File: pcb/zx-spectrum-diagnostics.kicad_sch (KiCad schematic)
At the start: 18 parts, among them U101 Pico, U102 ICL7660, U103 LM321

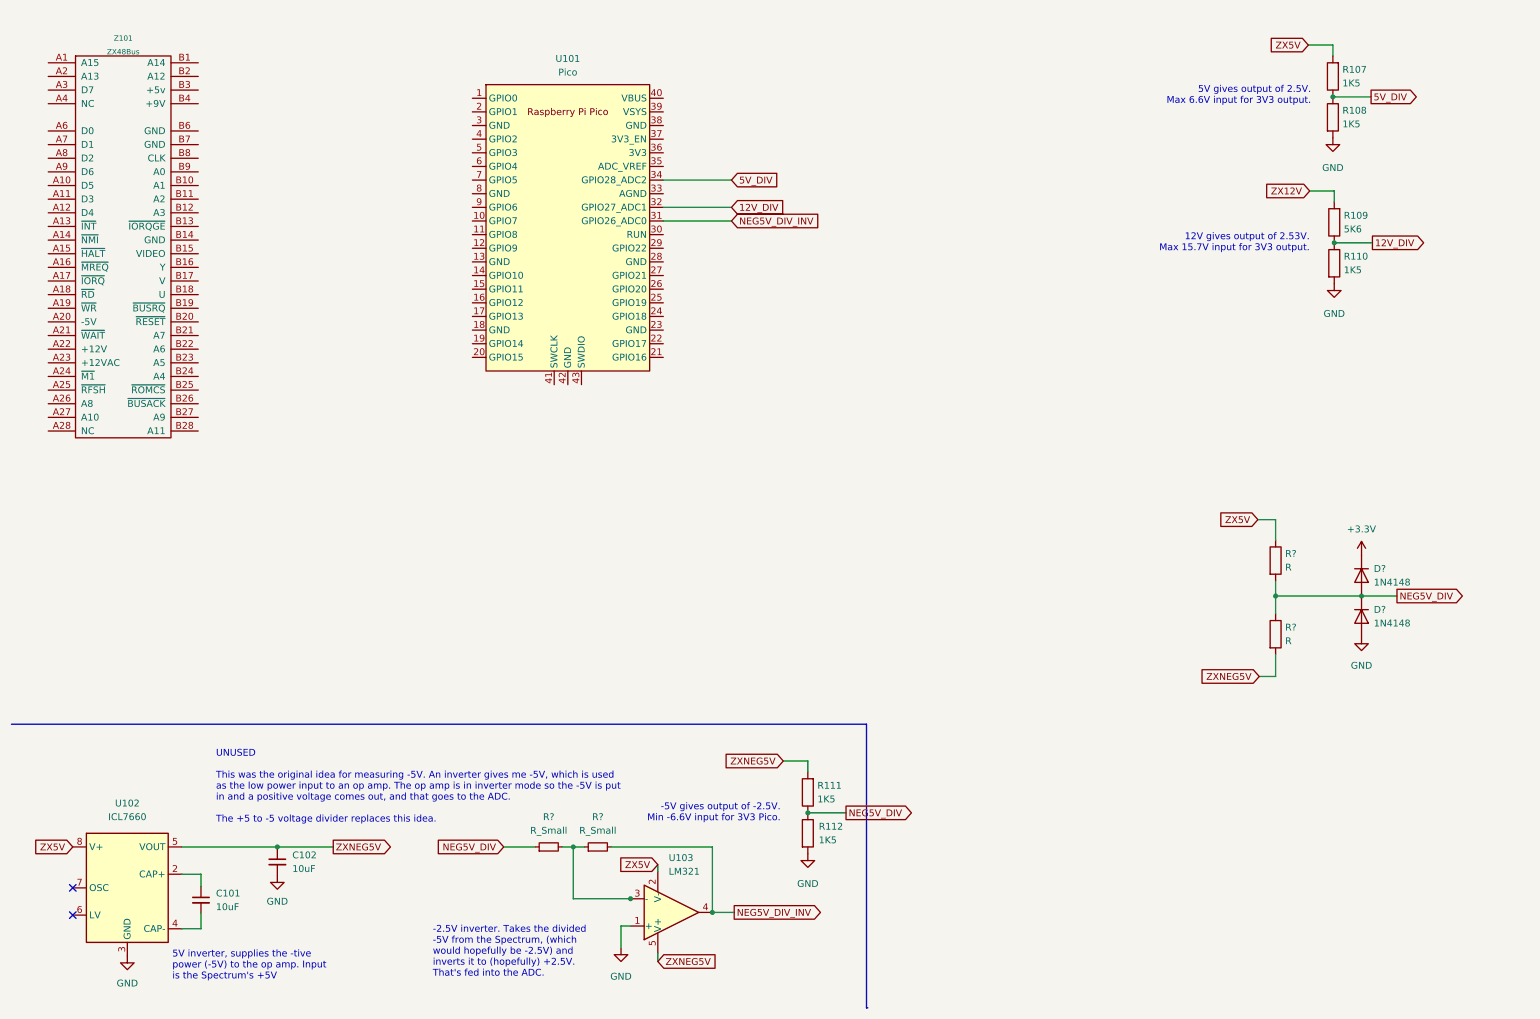
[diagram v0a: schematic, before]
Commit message: update schematic, add a second pico, tidy -5V sampler
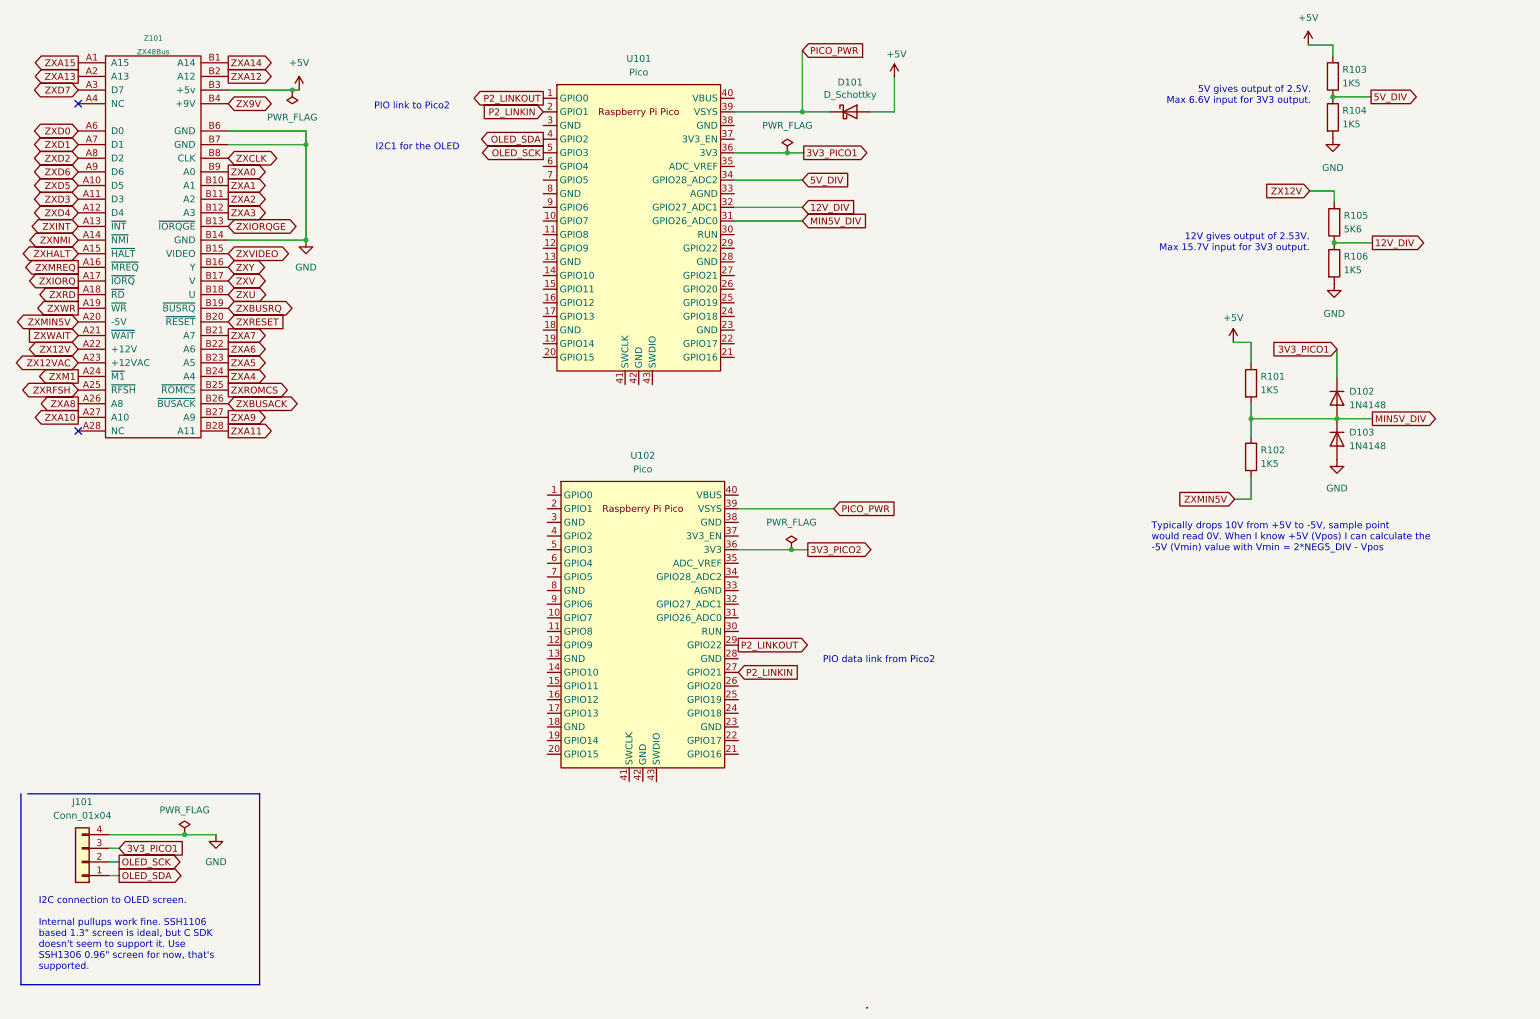
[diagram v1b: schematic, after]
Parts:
- removed C101, C102: 10uF, symbol Device:C_Small
- removed R111, R112: 1K5, symbol Device:R
- removed R? (x2): R_Small, symbol Device:R_Small
- removed U102: ICL7660, Package_SO:SOIC-8-N7_3.9x4.9mm_P1.27mm, symbol Regulator_SwitchedCapacitor:ICL7660
- removed U103: LM321, Package_TO_SOT_SMD:SOT-23-5, symbol Amplifier_Operational:LM321
- added D101: D_Schottky, Diode_SMD:D_1206_3216Metric_Pad1.42x1.75mm_HandSolder, symbol Device:D_Schottky
- added J101: Conn_01x04, symbol Connector_Generic:Conn_01x04
- added U102: Pico, RPi_Pico:RPi_Pico_SMD_TH, symbol Pico:Pico
- R101, R102: renamed from R?; value R -> 1K5
- gave numbers to parts that had none: 2
- renumbered R107 to R103, R108 to R104, R109 to R105, R110 to R106
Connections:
- net +3.3V is gone; now on net 3V3_PICO1: D102.1 (K)
- net NEG5V_DIV_INV is gone; now on net MIN5V_DIV: U101.31 (GPIO26_ADC0)
- net ZX5V is gone; now on net +5V: R101.1, R103.2
- net ZXNEG5V is gone; now on net ZXMIN5V: R102.2
- net GND: now also Z101.B14 (GND), Z101.B6 (GND), Z101.B7 (GND), J101.4 (Pin_4)
- net ZX12V: now also Z101.A22 (+12V)
- net ZXA15: now reaches Z101.A1 (A15)
- net ZXD5: now reaches Z101.A10 (D5)
- net ZXD3: now reaches Z101.A11 (D3)
- net ZXD4: now reaches Z101.A12 (D4)
- net ZXINT: now reaches Z101.A13 (~{INT})
- net ZXNMI: now reaches Z101.A14 (~{NMI})
- net ZXHALT: now reaches Z101.A15 (~{HALT})
- net ZXMREQ: now reaches Z101.A16 (~{MREQ})
- net ZXIORQ: now reaches Z101.A17 (~{IORQ})
- net ZXRD: now reaches Z101.A18 (~{RD})
- net ZXWR: now reaches Z101.A19 (~{WR})
- net ZXA13: now reaches Z101.A2 (A13)
- net ZXMIN5V: now reaches Z101.A20 (-5V)
- net ZXWAIT: now reaches Z101.A21 (~{WAIT})
- net ZX12VAC: now reaches Z101.A23 (+12VAC)
- net ZXM1: now reaches Z101.A24 (~{M1})
- net ZXRFSH: now reaches Z101.A25 (~{RFSH})
- net ZXA8: now reaches Z101.A26 (A8)
- net ZXA10: now reaches Z101.A27 (A10)
- net ZXD7: now reaches Z101.A3 (D7)
- net ZXD0: now reaches Z101.A6 (D0)
- net ZXD1: now reaches Z101.A7 (D1)
- net ZXD2: now reaches Z101.A8 (D2)
- net ZXD6: now reaches Z101.A9 (D6)
- net ZXA14: now reaches Z101.B1 (A14)
- net ZXA1: now reaches Z101.B10 (A1)
- net ZXA2: now reaches Z101.B11 (A2)
- net ZXA3: now reaches Z101.B12 (A3)
- net ZXIORQGE: now reaches Z101.B13 (~{IORQGE})
- net ZXVIDEO: now reaches Z101.B15 (VIDEO)
- net ZXY: now reaches Z101.B16 (Y)
- net ZXV: now reaches Z101.B17 (V)
- net ZXU: now reaches Z101.B18 (U)
- net ZXBUSRQ: now reaches Z101.B19 (~{BUSRQ})
- net ZXA12: now reaches Z101.B2 (A12)
- net ZXRESET: now reaches Z101.B20 (~{RESET})
- net ZXA7: now reaches Z101.B21 (A7)
- net ZXA6: now reaches Z101.B22 (A6)
- net ZXA5: now reaches Z101.B23 (A5)
- net ZXA4: now reaches Z101.B24 (A4)
- net ZXROMCS: now reaches Z101.B25 (~{ROMCS})
- net ZXBUSACK: now reaches Z101.B26 (~{BUSACK})
- net ZXA9: now reaches Z101.B27 (A9)
- net ZXA11: now reaches Z101.B28 (A11)
- net +5V: now reaches Z101.B3 (+5v)
- net +5V: now also D101.2 (A)
- net ZX9V: now reaches Z101.B4 (+9V)
- net ZXCLK: now reaches Z101.B8 (CLK)
- net ZXA0: now reaches Z101.B9 (A0)
- net P2_LINKOUT: now reaches U101.1 (GPIO0)
- net P2_LINKOUT: now also U102.29 (GPIO22)
- net P2_LINKIN: now reaches U101.2 (GPIO1)
- net P2_LINKIN: now also U102.27 (GPIO21)
- net 3V3_PICO1: now reaches U101.36 (3V3)
- net 3V3_PICO1: now also J101.3 (Pin_3)
- net PICO_PWR: now reaches U101.39 (VSYS)
- net PICO_PWR: now also D101.1 (K), U102.39 (VSYS)
- net OLED_SDA: now reaches U101.4 (GPIO2)
- net OLED_SDA: now also J101.1 (Pin_1)
- net OLED_SCK: now reaches U101.5 (GPIO3)
- net OLED_SCK: now also J101.2 (Pin_2)
- net NEG5V_DIV renamed MIN5V_DIV
- new net 3V3_PICO2: U102.36 (3V3)
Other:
- note added: "I2C connection to OLED screen. Internal pullups work fine. SSH1106 based 1.3" screen is ideal, but C SDK doesn't seem to support it. Use SSH1306 0.96" screen for now, that's supported."
- note added: "I2C1 for the OLED"
- note added: "PIO data link from Pico2"
- note added: "PIO link to Pico2"
- note added: "Typically drops 10V from +5V to -5V, sample point would read 0V. When I know +5V (Vpos) I can calculate the -5V (Vmin) value with Vmin = 2*NEG5_DIV - Vpos"
- note removed: "-2.5V inverter. Takes the divided -5V from the Spectrum, (which would hopefully be -2.5V) and inverts it to (hopefully) +2.5V. That's fed into the ADC."
- note removed: "-5V gives output of -2.5V. Min -6.6V input for 3V3 Pico."
- note removed: "5V inverter, supplies the -tive power (-5V) to the op amp. Input is the Spectrum's +5V"
- note removed: "UNUSED This was the original idea for measuring -5V. An inverter gives me -5V, which is used as the low power input to an op amp. The op amp is in inverter mode so the -5V is put in and a positive voltage comes out, and that goes to the ADC. The +5 to -5 voltage divider replaces this idea."
- moved on the sheet: D102, D103, R101, R102, U101, Z101

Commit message: first layout
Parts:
- D102, D103: footprint Diode_THT:D_DO-35_SOD27_P7.62mm_Horizontal -> Diode_SMD:D_1206_3216Metric_Pad1.42x1.75mm_HandSolder
- J101: footprint (none) -> Connector_PinHeader_2.54mm:PinHeader_1x04_P2.54mm_Vertical
- R101, R102, R103, R104, R105, R106: footprint (none) -> Resistor_SMD:R_1206_3216Metric_Pad1.30x1.75mm_HandSolder
- U101, U102: footprint RPi_Pico:RPi_Pico_SMD_TH -> Pico:RPi_Pico_SMD_TH
- Z101: footprint (none) -> zxbus:ZX_Bus_Pin_Header
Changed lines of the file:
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@@
   (title_block
     (title "ZX Spectrum Diagnostics Board")
-    (date "2023-08-27")
+    (date "2023-10-29")
   )
   (junction (at 67.818 37.592) (diameter 0) (color 0 0 0 0)
@@
       (effects (font (size 0.9906 0.9906)))
     )
-    (property "Footprint" "" (id 2) (at 30.48 103.632 0)
+    (property "Footprint" "zxbus:ZX_Bus_Pin_Header" (id 2) (at 30.48 103.632 0)
       (effects (font (size 0.9906 0.9906)) hide)
     )
@@
     (property "Reference" "J101" (id 0) (at 26.162 160.02 0))
     (property "Value" "Conn_01x04" (id 1) (at 26.162 162.56 0))
-    (property "Footprint" "" (id 2) (at 26.162 171.196 0)
+    (property "Footprint" "Connector_PinHeader_2.54mm:PinHeader_1x04_P2.54mm_Vertical" (id 2) (at 26.162 171.196 0)
       (effects (font (size 1.27 1.27)) hide)
     )
@@
     (property "Reference" "U101" (id 0) (at 129.794 21.59 0))
     (property "Value" "Pico" (id 1) (at 129.794 24.13 0))
-    (property "Footprint" "RPi_Pico:RPi_Pico_SMD_TH" (id 2) (at 129.794 53.086 90)
+    (property "Footprint" "Pico:RPi_Pico_SMD_TH" (id 2) (at 129.794 53.086 90)
       (effects (font (size 1.27 1.27)) hide)
     )
@@
       (effects (font (size 1.27 1.27)) (justify right))
     )
-    (property "Footprint" "" (id 2) (at 261.112 52.07 90)
+    (property "Footprint" "Resistor_SMD:R_1206_3216Metric_Pad1.30x1.75mm_HandSolder" (id 2) (at 261.112 52.07 90)
       (effects (font (size 1.27 1.27)) hide)
     )
@@
     (property "Reference" "U102" (id 0) (at 130.556 95.504 0))
     (property "Value" "Pico" (id 1) (at 130.556 98.044 0))
-    (property "Footprint" "RPi_Pico:RPi_Pico_SMD_TH" (id 2) (at 130.556 127 90)
+    (property "Footprint" "Pico:RPi_Pico_SMD_TH" (id 2) (at 130.556 127 90)
       (effects (font (size 1.27 1.27)) hide)
     )
@@
       (effects (font (size 1.27 1.27)) (justify right))
     )
-    (property "Footprint" "" (id 2) (at 260.858 24.892 90)
+    (property "Footprint" "Resistor_SMD:R_1206_3216Metric_Pad1.30x1.75mm_HandSolder" (id 2) (at 260.858 24.892 90)
       (effects (font (size 1.27 1.27)) hide)
     )
@@
       (effects (font (size 1.27 1.27)) (justify left))
     )
-    (property "Footprint" "Diode_THT:D_DO-35_SOD27_P7.62mm_Horizontal" (id 2) (at 259.842 92.456 0)
+    (property "Footprint" "Diode_SMD:D_1206_3216Metric_Pad1.42x1.75mm_HandSolder" (id 2) (at 259.842 92.456 0)
       (effects (font (size 1.27 1.27)) hide)
     )
@@
       (effects (font (size 1.27 1.27)) (justify left))
     )
-    (property "Footprint" "Diode_THT:D_DO-35_SOD27_P7.62mm_Horizontal" (id 2) (at 259.842 84.836 0)
+    (property "Footprint" "Diode_SMD:D_1206_3216Metric_Pad1.42x1.75mm_HandSolder" (id 2) (at 259.842 84.836 0)
       (effects (font (size 1.27 1.27)) hide)
     )
@@
       (effects (font (size 1.27 1.27)) (justify left))
     )
-    (property "Footprint" "" (id 2) (at 242.062 95.758 90)
+    (property "Footprint" "Resistor_SMD:R_1206_3216Metric_Pad1.30x1.75mm_HandSolder" (id 2) (at 242.062 95.758 90)
       (effects (font (size 1.27 1.27)) hide)
     )
@@
       (effects (font (size 1.27 1.27)) (justify left))
     )
-    (property "Footprint" "" (id 2) (at 257.302 32.512 90)
+    (property "Footprint" "Resistor_SMD:R_1206_3216Metric_Pad1.30x1.75mm_HandSolder" (id 2) (at 257.302 32.512 90)
       (effects (font (size 1.27 1.27)) hide)
     )
@@
       (effects (font (size 1.27 1.27)) (justify left))
     )
-    (property "Footprint" "" (id 2) (at 242.062 82.042 90)
+    (property "Footprint" "Resistor_SMD:R_1206_3216Metric_Pad1.30x1.75mm_HandSolder" (id 2) (at 242.062 82.042 90)
       (effects (font (size 1.27 1.27)) hide)
     )
@@
       (effects (font (size 1.27 1.27)) (justify left))
     )
-    (property "Footprint" "" (id 2) (at 257.556 59.69 90)
+    (property "Footprint" "Resistor_SMD:R_1206_3216Metric_Pad1.30x1.75mm_HandSolder" (id 2) (at 257.556 59.69 90)
       (effects (font (size 1.27 1.27)) hide)
     )
@@
     )
     (path "/d9d4c412-10f6-47b7-9c11-43e0dd422b75"
-      (reference "D102") (unit 1) (value "1N4148") (footprint "Diode_THT:D_DO-35_SOD27_P7.62mm_Horizontal")
+      (reference "D102") (unit 1) (value "1N4148") (footprint "Diode_SMD:D_1206_3216Metric_Pad1.42x1.75mm_HandSolder")
     )
     (path "/d3364c3f-7456-4539-86a5-d88591e950f5"
-      (reference "D103") (unit 1) (value "1N4148") (footprint "Diode_THT:D_DO-35_SOD27_P7.62mm_Horizontal")
+      (reference "D103") (unit 1) (value "1N4148") (footprint "Diode_SMD:D_1206_3216Metric_Pad1.42x1.75mm_HandSolder")
     )
     (path "/4306a88c-b446-420a-8a4d-c6b820db0ec2"
-      (reference "J101") (unit 1) (value "Conn_01x04") (footprint "")
+      (reference "J101") (unit 1) (value "Conn_01x04") (footprint "Connector_PinHeader_2.54mm:PinHeader_1x04_P2.54mm_Vertical")
     )
     (path "/f338c199-5c84-47b5-961e-f046c86e3290"
-      (reference "R101") (unit 1) (value "1K5") (footprint "")
+      (reference "R101") (unit 1) (value "1K5") (footprint "Resistor_SMD:R_1206_3216Metric_Pad1.30x1.75mm_HandSolder")
     )
     (path "/e1ce659c-6ff5-46ac-8196-738a93ea61ec"
-      (reference "R102") (unit 1) (value "1K5") (footprint "")
+      (reference "R102") (unit 1) (value "1K5") (footprint "Resistor_SMD:R_1206_3216Metric_Pad1.30x1.75mm_HandSolder")
     )
     (path "/ceb09983-1f41-4d0f-bb1d-6819cfe3f40b"
-      (reference "R103") (unit 1) (value "1K5") (footprint "")
+      (reference "R103") (unit 1) (value "1K5") (footprint "Resistor_SMD:R_1206_3216Metric_Pad1.30x1.75mm_HandSolder")
     )
     (path "/efd02726-493f-4f8f-8388-70de053feda7"
-      (reference "R104") (unit 1) (value "1K5") (footprint "")
+      (reference "R104") (unit 1) (value "1K5") (footprint "Resistor_SMD:R_1206_3216Metric_Pad1.30x1.75mm_HandSolder")
     )
     (path "/5b9033e9-4560-4357-b6ad-41da0b364e3d"
-      (reference "R105") (unit 1) (value "5K6") (footprint "")
+      (reference "R105") (unit 1) (value "5K6") (footprint "Resistor_SMD:R_1206_3216Metric_Pad1.30x1.75mm_HandSolder")
     )
     (path "/fec3f67f-cd37-4f72-a82c-c01b7e5ac127"
-      (reference "R106") (unit 1) (value "1K5") (footprint "")
+      (reference "R106") (unit 1) (value "1K5") (footprint "Resistor_SMD:R_1206_3216Metric_Pad1.30x1.75mm_HandSolder")
     )
     (path "/5510a4fe-1794-434f-b7d2-120f1084055a"
-      (reference "U101") (unit 1) (value "Pico") (footprint "RPi_Pico:RPi_Pico_SMD_TH")
+      (reference "U101") (unit 1) (value "Pico") (footprint "Pico:RPi_Pico_SMD_TH")
     )
     (path "/608ee8f9-b792-4f57-b8f2-f79ae2550fbc"
-      (reference "U102") (unit 1) (value "Pico") (footprint "RPi_Pico:RPi_Pico_SMD_TH")
+      (reference "U102") (unit 1) (value "Pico") (footprint "Pico:RPi_Pico_SMD_TH")
     )
     (path "/28a893db-1c35-4c03-b308-f54ebb07c369"
-      (reference "Z101") (unit 1) (value "ZX48Bus") (footprint "")
-    )
-  )
+      (reference "Z101") (unit 1) (value "ZX48Bus") (footprint "zxbus:ZX_Bus_Pin_Header")
+    )
+  )
